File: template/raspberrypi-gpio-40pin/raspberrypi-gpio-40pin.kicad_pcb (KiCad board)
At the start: 2 copper layers, 65 x 56 mm, 5 parts, among them P1 CONN_02X20

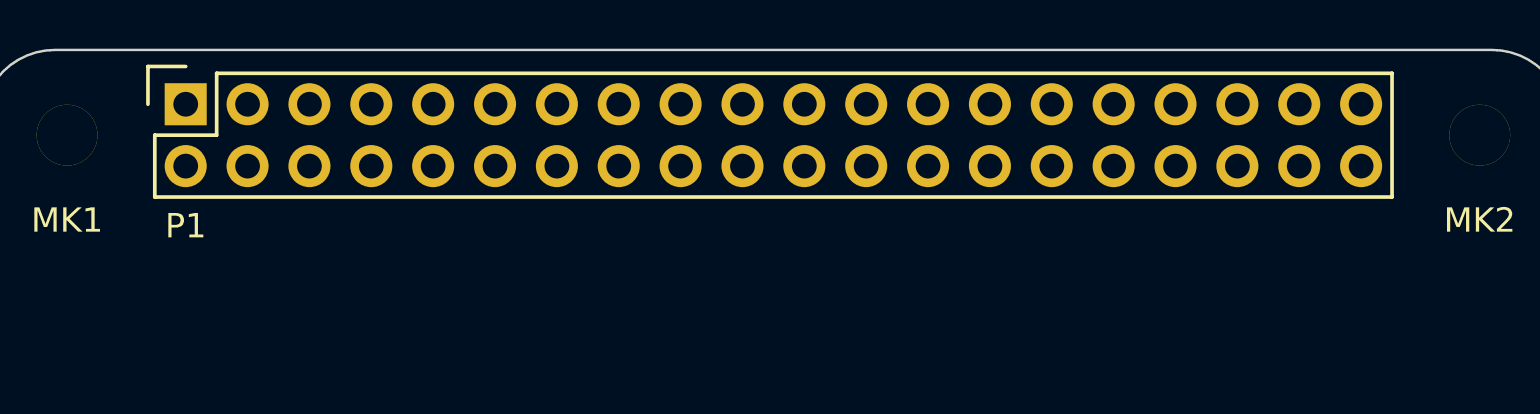
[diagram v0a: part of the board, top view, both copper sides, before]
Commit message: Flipped GPIO header on board so that pin one is in the correct position
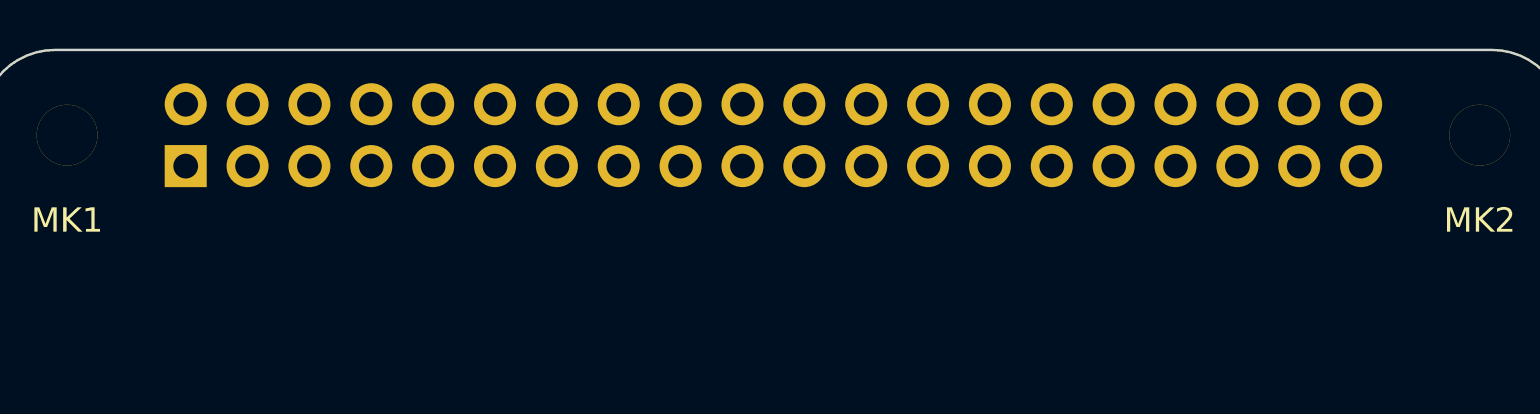
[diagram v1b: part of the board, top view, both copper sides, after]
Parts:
- P1: moved to B.Cu
- moved P1 2.54 mm to (208.4, 98.8)

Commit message: fixed pinout in PCB by actually reading the netlist
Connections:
- P1 pad 36: /GPIO20 -> /GPIO16
- P1 pad 38: /GPIO21 -> /GPIO20
- P1 pad 40: GND -> /GPIO21
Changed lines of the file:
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@@
 (kicad_pcb (version 4) (host pcbnew 4.0.6)
   (general
-    (links 10)
-    (no_connects 10)
-    (area 199.949999 92.155 287.050001 168.06)
+    (links 9)
+    (no_connects 9)
+    (area 199.949999 93.949999 265.050001 150.050001)
     (thickness 1.6)
     (drawings 39)
@@
     (zones 0)
     (modules 5)
-    (nets 31)
+    (nets 32)
   )
   (page A3)
@@
   (net 29 "/GPIO8(SPI_CE0_N)")
   (net 30 "/GPIO7(SPI_CE1_N)")
+  (net 31 /GPIO16)
   (net_class Default "This is the default net class."
     (clearance 0.2)
@@
     (add_net "/GPIO14(TXD0)")
     (add_net "/GPIO15(RXD0)")
+    (add_net /GPIO16)
     (add_net "/GPIO17(GEN0)")
     (add_net "/GPIO18(GEN1)")
@@
       (net 10 /GPIO19))
     (pad 36 thru_hole oval (at 43.18 -2.54) (size 1.7272 1.7272) (drill 1.016) (layers *.Cu *.Mask B.SilkS)
-      (net 11 /GPIO20))
+      (net 31 /GPIO16))
     (pad 37 thru_hole oval (at 45.72 0) (size 1.7272 1.7272) (drill 1.016) (layers *.Cu *.Mask B.SilkS)
       (net 12 /GPIO26))
     (pad 38 thru_hole oval (at 45.72 -2.54) (size 1.7272 1.7272) (drill 1.016) (layers *.Cu *.Mask B.SilkS)
+      (net 11 /GPIO20))
+    (pad 39 thru_hole oval (at 48.26 0) (size 1.7272 1.7272) (drill 1.016) (layers *.Cu *.Mask B.SilkS)
+      (net 3 GND))
+    (pad 40 thru_hole oval (at 48.26 -2.54) (size 1.7272 1.7272) (drill 1.016) (layers *.Cu *.Mask B.SilkS)
       (net 13 /GPIO21))
-    (pad 39 thru_hole oval (at 48.26 0) (size 1.7272 1.7272) (drill 1.016) (layers *.Cu *.Mask B.SilkS)
-      (net 3 GND))
-    (pad 40 thru_hole oval (at 48.26 -2.54) (size 1.7272 1.7272) (drill 1.016) (layers *.Cu *.Mask B.SilkS)
-      (net 3 GND))
     (model Socket_Strips.3dshapes/Socket_Strip_Straight_2x20.wrl
       (at (xyz 0.95 -0.05 0))
